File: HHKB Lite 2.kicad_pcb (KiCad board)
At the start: 2 copper layers, 72.4 x 48 mm, 3 parts, among them U1 Teensy2.0_(C)

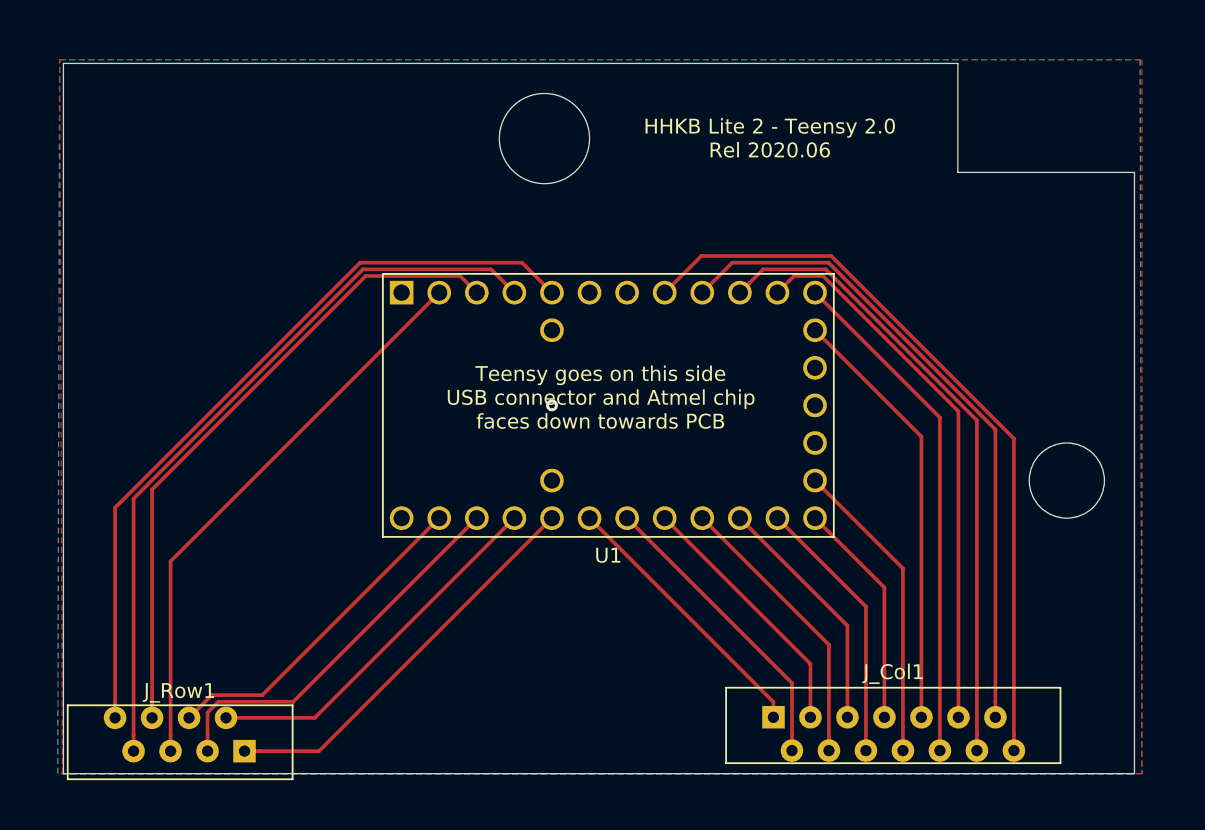
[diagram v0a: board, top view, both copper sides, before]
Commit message: Teensy 2.0 -> Pi Pico, sent to fab
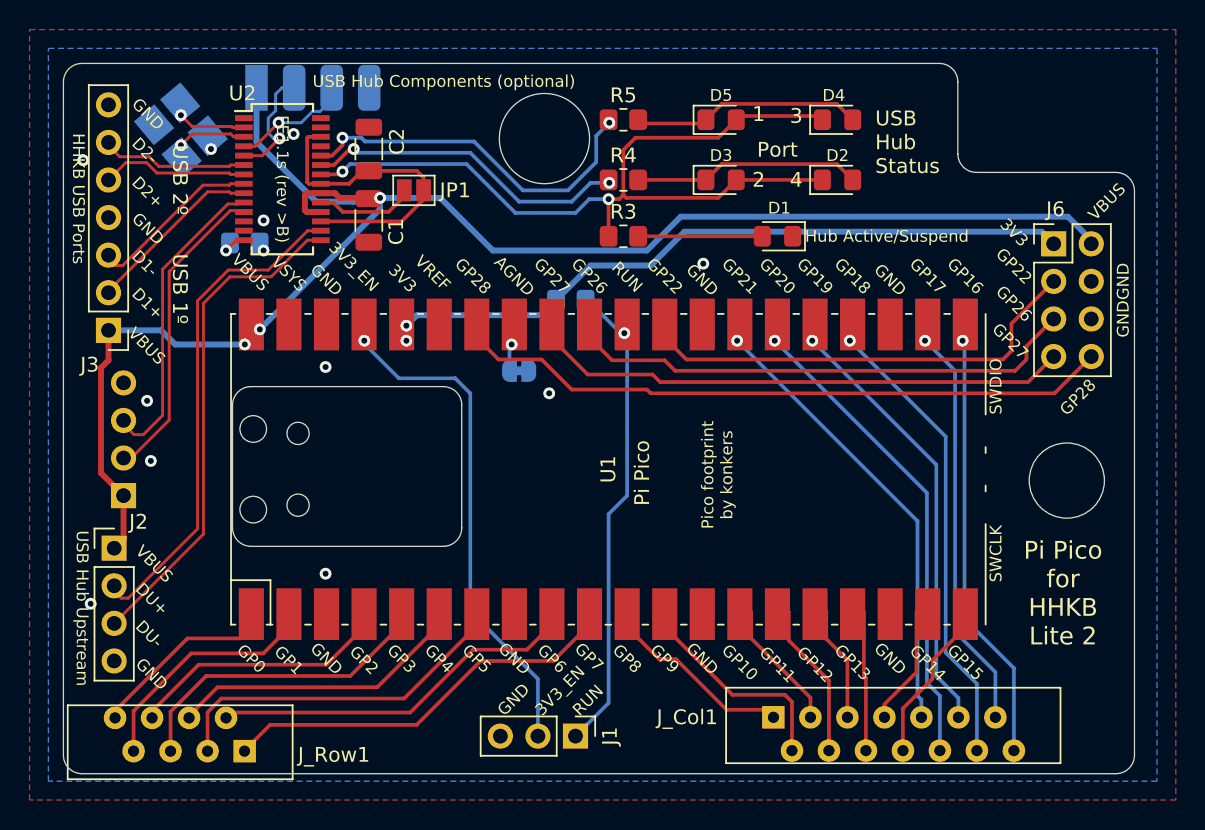
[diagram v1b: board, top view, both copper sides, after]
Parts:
- added C1: 10uF, Capacitor_SMD:C_1206_3216Metric, F.Cu at (142.6, 39.6)
- added C2: 10uF, Capacitor_SMD:C_1206_3216Metric, F.Cu at (142.6, 34.7)
- added D1: LED, LED_SMD:LED_0805_2012Metric_Pad1.15x1.40mm_HandSolder, F.Cu at (170.2, 40.6)
- added D2: LED, LED_SMD:LED_0805_2012Metric_Pad1.15x1.40mm_HandSolder, F.Cu at (174.2, 36.8)
- added D3: LED, LED_SMD:LED_0805_2012Metric_Pad1.15x1.40mm_HandSolder, F.Cu at (166.4, 36.8)
- added D4: LED, LED_SMD:LED_0805_2012Metric_Pad1.15x1.40mm_HandSolder, F.Cu at (174.2, 32.8)
- added D5: LED, LED_SMD:LED_0805_2012Metric_Pad1.15x1.40mm_HandSolder, F.Cu at (166.4, 32.8)
- added J1: Conn_01x02_Male, Connector_PinHeader_2.54mm:PinHeader_1x03_P2.54mm_Vertical, F.Cu at (156.5, 74.4)
- added J2: Conn_01x02_Male, Connector_PinHeader_2.54mm:PinHeader_1x04_P2.54mm_Vertical, F.Cu at (125.3, 61.7)
- added J3: Conn_01x07_Male, Connector_PinHeader_2.54mm:PinHeader_1x07_P2.54mm_Vertical, F.Cu at (125.0, 47.0)
- added J4: Conn_01x04_Male, Connector_PinHeader_2.54mm:PinHeader_1x04_P2.54mm_Vertical, B.Cu at (126.0, 58.2)
- added J5: Conn_01x02_Male, Connector_PinHeader_2.54mm:2.54mm 1x4 header edge, B.Cu at (133.7, 29.0)
- added J6: Conn_01x07_Male, Connector_PinHeader_2.54mm:PinHeader_2x04_P2.54mm_Vertical, F.Cu at (188.8, 41.1)
- added JP1: Jumper-2_P1.3mm_Open_Pad1.0x1.5mm, Jumper:SolderJumper-2_P1.3mm_Open_Pad1.0x1.5mm, F.Cu at (145.6, 37.5)
- added JP2: Jumper_2_Bridged, Jumper:SolderJumper-2_P1.3mm_Bridged_RoundedPad1.0x1.5mm, B.Cu at (152.7, 49.7)
- added R1: 4.7K, Resistor_SMD:R_0805_2012Metric_Pad1.20x1.40mm_HandSolder, B.Cu at (156.2, 45.0)
- added R2: 2.7K, Resistor_SMD:R_0805_2012Metric_Pad1.20x1.40mm_HandSolder, B.Cu at (134.2, 41.1)
- added R3: 330, Resistor_SMD:R_0805_2012Metric_Pad1.20x1.40mm_HandSolder, F.Cu at (159.8, 40.6)
- added R4: 330, Resistor_SMD:R_0805_2012Metric_Pad1.20x1.40mm_HandSolder, F.Cu at (159.8, 36.8)
- added R5: 330, Resistor_SMD:R_0805_2012Metric_Pad1.20x1.40mm_HandSolder, F.Cu at (159.8, 32.8)
- added U2: FE1.1s, Package_SO:SSOP-28_3.9x9.9mm_P0.635mm, F.Cu at (136.7, 36.8)
- added Y1: 12mhz, Crystal:Crystal_SMD_3225-4Pin_3.2x2.5mm_HandSoldering, B.Cu at (129.9, 33.5)
- U1: value Teensy2.0_(C) -> Pico; footprint teensy:Teensy2.0 -> MCU_RaspberryPi_and_Boards:RPi_Pico_SMD; moved to F.Cu
- moved U1 4.32 mm to (158.8, 56.4), turned to 90 degrees
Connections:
- U1 pad 1: GND -> Net-(J_Row1-Pad8)
- U1 pad 10: Net-(J_Col1-Pad12) -> Net-(J_Row1-Pad1)
- U1 pad 11: Net-(J_Col1-Pad11) -> Net-(J_Col1-Pad1)
- U1 pad 12: Net-(J_Col1-Pad10) -> Net-(J_Col1-Pad2)
- U1 pad 13: Net-(J_Col1-Pad9) -> GND
- U1 pad 14: (no net) -> Net-(J_Col1-Pad3)
- U1 pad 15: GND -> Net-(J_Col1-Pad4)
- U1 pad 16: (no net) -> Net-(J_Col1-Pad5)
- U1 pad 17: Net-(J_Col1-Pad8) -> Net-(J_Col1-Pad6)
- U1 pad 18: Net-(J_Col1-Pad7) -> GND
- U1 pad 19: Net-(J_Col1-Pad6) -> Net-(J_Col1-Pad7)
- U1 pad 2: Net-(J_Row1-Pad5) -> Net-(J_Row1-Pad7)
- U1 pad 20: Net-(J_Col1-Pad5) -> Net-(J_Col1-Pad8)
- U1 pad 21: Net-(J_Col1-Pad4) -> Net-(J_Col1-Pad14)
- U1 pad 22: Net-(J_Col1-Pad3) -> Net-(J_Col1-Pad13)
- U1 pad 23: Net-(J_Col1-Pad2) -> GND
- U1 pad 24: Net-(J_Col1-Pad1) -> Net-(J_Col1-Pad12)
- U1 pad 25: Net-(J_Row1-Pad1) -> Net-(J_Col1-Pad11)
- U1 pad 26: Net-(J_Row1-Pad2) -> Net-(J_Col1-Pad10)
- U1 pad 27: Net-(J_Row1-Pad3) -> Net-(J_Col1-Pad9)
- U1 pad 28: Net-(J_Row1-Pad4) -> GND
- U1 pad 29: (no net) -> GPIO22
- U1 pad 3: Net-(J_Row1-Pad6) -> GND
- U1 pad 30: (no net) -> RESET_H
- U1 pad 31: (no net) -> GPIP26
- U1 pad 4: Net-(J_Row1-Pad7) -> Net-(J_Row1-Pad6)
- U1 pad 5: Net-(J_Row1-Pad8) -> Net-(J_Row1-Pad5)
- U1 pad 6: (no net) -> Net-(J_Row1-Pad4)
- U1 pad 7: (no net) -> Net-(J_Row1-Pad3)
- U1 pad 8: Net-(J_Col1-Pad14) -> GND
- U1 pad 9: Net-(J_Col1-Pad13) -> Net-(J_Row1-Pad2)
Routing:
- net VBUS: track 0.00 -> 111.4 mm, vias 0 -> 3
- net DRV: track 0.00 -> 56.0 mm, vias 0 -> 2
- net +3V3: track 0.00 -> 47.7 mm, vias 0 -> 2
- net GPIO28: track 0.00 -> 44.1 mm
- net Net-(J_Row1-Pad8): track 51.4 -> 11.5 mm
- net GPIO27: track 0.00 -> 35.9 mm
- net Net-(J_Row1-Pad7): track 49.9 -> 15.5 mm
- net GPIP26: track 0.00 -> 34.3 mm
- net DU+: track 0.00 -> 33.8 mm
- net DU-: track 0.00 -> 33.8 mm
- net 3V3_EN_H: track 0.00 -> 33.8 mm, vias 0 -> 1
- net RESET_H: track 0.00 -> 32.2 mm, vias 0 -> 1
- net GPIO22: track 0.00 -> 30.2 mm
- net Net-(J_Row1-Pad6): track 43.8 -> 16.7 mm
- net LED2: track 0.00 -> 24.7 mm, vias 0 -> 2
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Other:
- outline, holes or cut-outs redrawn
- net class Default removed
- board text added: "1"
- board text added: "2"
- board text added: "3"
- board text added: "3V3"
- board text added: "3V3_EN"
- board text added: "4"
- board text added: "AGND to GND"
- board text added: "Cutout for access to Test Points TP1-TP6"
- board text added: "D1+"
- board text added: "D1-"
- board text added: "D2+"
- board text added: "D2-"
- board text added: "D3+"
- board text added: "D3-"
- board text added: "D4+"
- board text added: "D4-"
- board text added: "DU+"
- board text added: "DU-"
- board text added: "FE1.1s (rev >B)"
- board text added: "Free GPIOs! Take One!"
- board text added: "GND"
- board text added: "GP22"
- board text added: "GP26"
- board text added: "GP27"
- board text added: "GP28"
- board text added: "HHKB USB Ports"
- board text added: "Hub Active/Suspend"
- board text added: "JP1 - USB Hub Power Mode Closed: hub is Self-Powered via separate power supply Open: (default) hub is Bus-Powered via USB uplink (J2 VBUS), max 100mA/port"
- board text added: "Only required components are U1 (Pi Pico), J_Row1 and J_Col1 All other components are for an optional USB hub that will allow the built-in USB ports to function, or external reset button (R1 and J1)."
- board text added: "Pi Pico"
- board text added: "Pi Pico for HHKB Lite 2"
- board text added: "Pico footprint by konkers"
- board text added: "Port"
- board text added: "RUN"
- board text added: "Rel 2024.06 - github.com/xunker"
- board text added: "TEST POINT ACCESS"
- board text added: "TP2"
- board text added: "TP3"
- board text added: "To Pi Pico USB Test Points or Cable"
- board text added: "USB 1º"
- board text added: "USB 2º"
- board text added: "USB 3º"
- board text added: "USB 4º (Bonus!)"
- board text added: "USB Hub Components (optional)"
- board text added: "USB Hub Status"
- board text added: "USB Hub Upstream"
- board text added: "VBUS"
- board text added: "based on Teensy 2.0 ver by thriteen37"
- board text removed: "DO NOT MOUNT HERE"
- board text removed: "HHKB Lite 2 - Teensy 2.0 Rel 2020.06"
- board text removed: "Teensy goes on this side USB connector and Atmel chip faces down towards PCB"
